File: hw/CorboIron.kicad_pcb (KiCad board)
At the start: 2 copper layers, 78.7 x 99.1 mm, 101 parts, among them P1 CONN_01X03, P10 CONN_01X04, P11 CONN_01X04, P2 CONN_01X03, P3 CONN_01X03, P4 Arduino_nano, P5 CONN_01X03, P6 CONN_01X04, P7 CONN_01X02, P8 CONN_01X03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

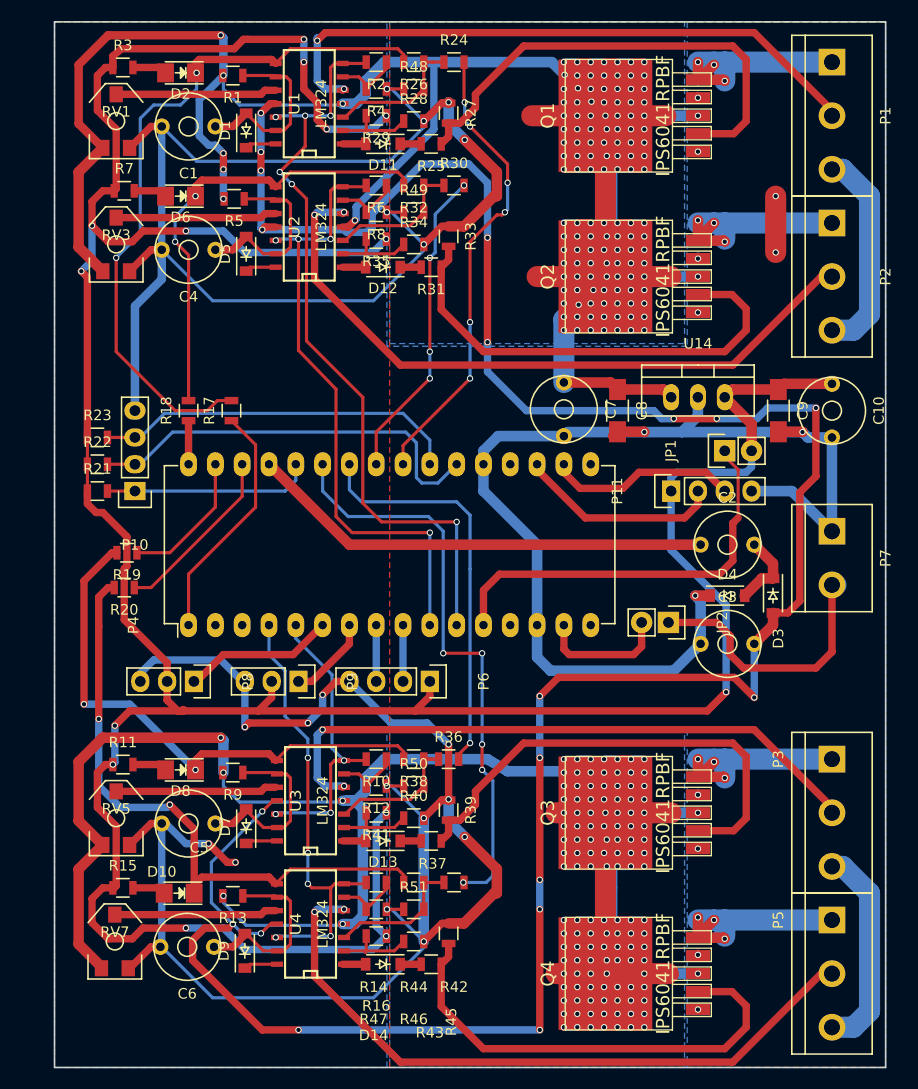
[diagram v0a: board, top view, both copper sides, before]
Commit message: Tidying up of silkscreen
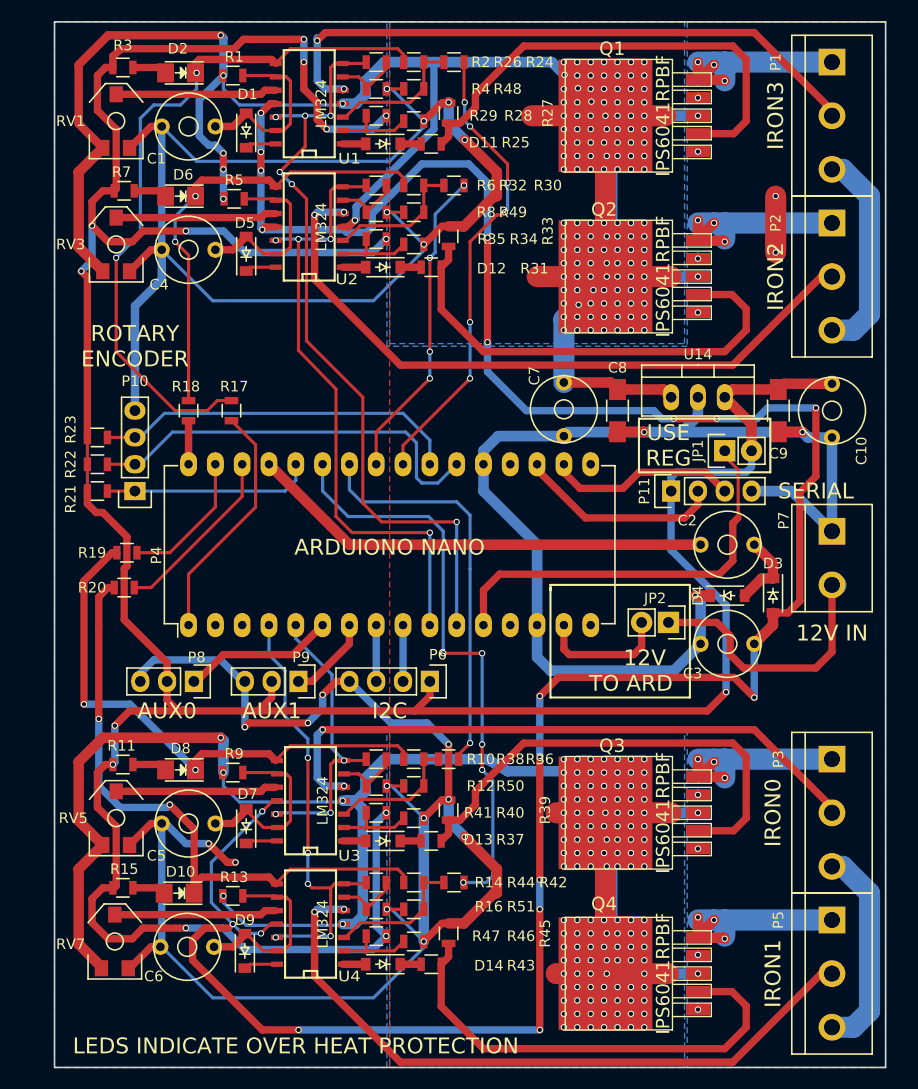
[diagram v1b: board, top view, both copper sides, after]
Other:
- board text added: "12V IN"
- board text added: "12V TO ARD"
- board text added: "ARDUIONO NANO"
- board text added: "AUX0"
- board text added: "AUX1"
- board text added: "I2C"
- board text added: "IRON0"
- board text added: "IRON1"
- board text added: "IRON2"
- board text added: "IRON3"
- board text added: "LEDS INDICATE OVER HEAT PROTECTION"
- board text added: "ROTARY ENCODER"
- board text added: "SERIAL"
- board text added: "USE REG"
